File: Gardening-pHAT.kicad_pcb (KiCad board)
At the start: 2 copper layers, 65 x 30 mm, 25 parts, among them P1 CONN_01X03, P2 CONN_01X03, P3 CONN_01X03, P4 CONN_02X05, U1 CAT24C32WI-GT3, U2 MCP3002

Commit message: Control 3.3V to sensors through GPIO
Connect the 3.3V of the soil moisture sensors
to GPIO5 and GPIO6 of Raspberry Pi. This way
the sensors will be enabled only during
measurement and their life will be significantly
increased.

Signed-off-by: Leon Anavi <leon@anavi.org>
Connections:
- P2 pad 3: +3V3 -> /GPIO6
- P3 pad 3: +3V3 -> /GPIO5
- RASP_CONN1 pad 29: (no net) -> /GPIO5
- RASP_CONN1 pad 31: (no net) -> /GPIO6
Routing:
- net /GPIO5: track 0.00 -> 25.5 mm
- net /GPIO6: track 0.00 -> 25.1 mm
- net +3V3: track 170.8 -> 157.5 mm
- net Net-(RASP_CONN1-Pad19): track 22.8 -> 21.3 mm
- net Net-(R3-Pad2): track 35.5 -> 35.0 mm
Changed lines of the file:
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@@
     (thickness 1.6)
     (drawings 32)
-    (tracks 267)
+    (tracks 273)
     (zones 0)
     (modules 25)
-    (nets 23)
+    (nets 25)
   )
   (page A4)
@@
   (net 21 "Net-(D1-Pad2)")
   (net 22 "Net-(R4-Pad2)")
+  (net 23 /GPIO6)
+  (net 24 /GPIO5)
   (net_class Default "This is the default net class."
     (clearance 0.254)
@@
     (add_net +3V3)
     (add_net +5V)
+    (add_net /GPIO5)
+    (add_net /GPIO6)
     (add_net /RXD)
     (add_net /TXD)
@@
       (net 2 GND))
     (pad 3 thru_hole circle (at 10 3.5) (size 3 3) (drill 1.4) (layers *.Cu *.Mask F.SilkS)
-      (net 1 +3V3))
+      (net 23 /GPIO6))
   )
   (module Pin_Headers:Pin_Header_Straight_1x04 (layer F.Cu)
@@
     (pad 28 thru_hole oval (at 2.54 33.02 90) (size 1.7272 1.7272) (drill 1.016) (layers *.Cu *.Mask F.SilkS)
       (net 5 "Net-(R2-Pad2)"))
-    (pad 29 thru_hole oval (at 0 35.56 90) (size 1.7272 1.7272) (drill 1.016) (layers *.Cu *.Mask F.SilkS))
+    (pad 29 thru_hole oval (at 0 35.56 90) (size 1.7272 1.7272) (drill 1.016) (layers *.Cu *.Mask F.SilkS)
+      (net 24 /GPIO5))
     (pad 30 thru_hole oval (at 2.54 35.56 90) (size 1.7272 1.7272) (drill 1.016) (layers *.Cu *.Mask F.SilkS)
       (net 2 GND))
-    (pad 31 thru_hole oval (at 0 38.1 90) (size 1.7272 1.7272) (drill 1.016) (layers *.Cu *.Mask F.SilkS))
+    (pad 31 thru_hole oval (at 0 38.1 90) (size 1.7272 1.7272) (drill 1.016) (layers *.Cu *.Mask F.SilkS)
+      (net 23 /GPIO6))
     (pad 32 thru_hole oval (at 2.54 38.1 90) (size 1.7272 1.7272) (drill 1.016) (layers *.Cu *.Mask F.SilkS))
     (pad 33 thru_hole oval (at 0 40.64 90) (size 1.7272 1.7272) (drill 1.016) (layers *.Cu *.Mask F.SilkS))
@@
       (net 2 GND))
     (pad 3 thru_hole circle (at 10 3.5) (size 3 3) (drill 1.4) (layers *.Cu *.Mask F.SilkS)
-      (net 1 +3V3))
+      (net 24 /GPIO5))
   )
   (module myfootprint:KLEMA_1x3 (layer F.Cu)
@@
   (gr_arc (start 151.5011 102.0036) (end 148.5011 102.0036) (angle -90) (layer Edge.Cuts) (width 0.1))
   (gr_circle (center 152.0011 101.5036) (end 152.0011 101.5036) (layer Edge.Cuts) (width 0.1))
+  (segment (start 204.2795 84.455) (end 204.2795 85.0265) (width 0.5) (layer F.Cu) (net 1))
+  (segment (start 204.2795 85.0265) (end 199.898 89.408) (width 0.5) (layer F.Cu) (net 1))
+  (segment (start 176.6165 103.886) (end 173.8935 101.163) (width 0.5) (layer F.Cu) (net 1))
+  (segment (start 195.199 103.886) (end 176.6165 103.886) (width 0.5) (layer F.Cu) (net 1))
+  (segment (start 196.469 102.616) (end 195.199 103.886) (width 0.5) (layer F.Cu) (net 1))
+  (segment (start 196.469 99.695) (end 196.469 102.616) (width 0.5) (layer F.Cu) (net 1))
+  (segment (start 199.898 96.266) (end 196.469 99.695) (width 0.5) (layer F.Cu) (net 1))
+  (segment (start 199.898 89.408) (end 199.898 96.266) (width 0.5) (layer F.Cu) (net 1))
   (segment (start 159.893 93.134) (end 171.8905 93.134) (width 0.5) (layer F.Cu) (net 1))
   (segment (start 171.8905 93.134) (end 171.9335 93.091) (width 0.5) (layer F.Cu) (net 1))
@@
   (segment (start 157.7135 90.9545) (end 159.893 93.134) (width 0.5) (layer F.Cu) (net 1))
   (segment (start 159.893 93.134) (end 159.893 93.218) (width 0.5) (layer F.Cu) (net 1) (status 30))
-  (segment (start 173.934 101.163) (end 176.657 103.886) (width 0.5) (layer B.Cu) (net 1))
-  (segment (start 176.657 103.886) (end 186.22 103.886) (width 0.5) (layer B.Cu) (net 1))
-  (segment (start 186.22 103.886) (end 188.943 101.163) (width 0.5) (layer B.Cu) (net 1))
-  (segment (start 188.943 101.694) (end 191.135 103.886) (width 0.5) (layer B.Cu) (net 1))
-  (segment (start 201.333 103.886) (end 204.056 101.163) (width 0.5) (layer B.Cu) (net 1))
-  (segment (start 191.135 103.886) (end 201.333 103.886) (width 0.5) (layer B.Cu) (net 1))
-  (segment (start 204.056 101.163) (end 204.056 94.836) (width 0.5) (layer B.Cu) (net 1))
-  (segment (start 200.025 84.455) (end 204.2795 84.455) (width 0.5) (layer B.Cu) (net 1))
-  (segment (start 198.374 86.106) (end 200.025 84.455) (width 0.5) (layer B.Cu) (net 1))
-  (segment (start 198.374 89.154) (end 198.374 86.106) (width 0.5) (layer B.Cu) (net 1))
-  (segment (start 204.056 94.836) (end 198.374 89.154) (width 0.5) (layer B.Cu) (net 1))
   (segment (start 173.8935 101.163) (end 173.934 101.163) (width 0.5) (layer B.Cu) (net 1))
-  (segment (start 188.943 101.163) (end 188.943 101.694) (width 0.5) (layer B.Cu) (net 1))
   (segment (start 208.788 85.936) (end 208.788 88.816) (width 0.5) (layer F.Cu) (net 1))
   (segment (start 177.17 79.8) (end 177.17 88.8415) (width 0.5) (layer B.Cu) (net 1))
@@
   (segment (start 208.788 91.016) (end 204.3635 89.619) (width 0.5) (layer F.Cu) (net 5) (status 10))
   (segment (start 204.3635 89.619) (end 204.2795 89.535) (width 0.5) (layer F.Cu) (net 5) (status 30))
+  (segment (start 189.87 79.8) (end 189.87 81.158) (width 0.5) (layer F.Cu) (net 6))
+  (segment (start 202.184 89.9795) (end 204.2795 92.075) (width 0.5) (layer B.Cu) (net 6))
+  (segment (start 202.184 85.598) (end 202.184 89.9795) (width 0.5) (layer B.Cu) (net 6))
+  (segment (start 201.549 84.963) (end 202.184 85.598) (width 0.5) (layer B.Cu) (net 6))
+  (via (at 201.549 84.963) (size 0.85) (drill 0.4) (layers F.Cu B.Cu) (net 6))
+  (segment (start 198.628 82.042) (end 201.549 84.963) (width 0.5) (layer F.Cu) (net 6))
+  (segment (start 190.754 82.042) (end 198.628 82.042) (width 0.5) (layer F.Cu) (net 6))
+  (segment (start 189.87 81.158) (end 190.754 82.042) (width 0.5) (layer F.Cu) (net 6))
   (segment (start 204.2795 92.075) (end 204.343 92.075) (width 0.5) (layer B.Cu) (net 6))
   (segment (start 204.343 92.075) (end 210.312 86.106) (width 0.5) (layer B.Cu) (net 6))
@@
   (via (at 210.312 86.106) (size 0.85) (drill 0.4) (layers F.Cu B.Cu) (net 6))
   (segment (start 204.2795 92.075) (end 204.2795 91.8845) (width 0.5) (layer B.Cu) (net 6) (status 30))
-  (segment (start 204.2795 91.8845) (end 199.39 87.5665) (width 0.5) (layer B.Cu) (net 6) (status 10))
-  (segment (start 199.3265 87.503) (end 199.3265 82.6565) (width 0.5) (layer F.Cu) (net 6))
-  (segment (start 199.39 87.5665) (end 199.3265 87.503) (width 0.5) (layer F.Cu) (net 6))
-  (via (at 199.39 87.5665) (size 0.85) (drill 0.4) (layers F.Cu B.Cu) (net 6))
   (segment (start 204.2795 92.075) (end 204.2795 92.0115) (width 0.5) (layer B.Cu) (net 6) (status 30))
-  (segment (start 189.87 79.8) (end 189.87 81.9835) (width 0.5) (layer F.Cu) (net 6))
-  (segment (start 190.543 82.6565) (end 199.3265 82.6565) (width 0.5) (layer F.Cu) (net 6))
-  (segment (start 189.87 81.9835) (end 190.543 82.6565) (width 0.5) (layer F.Cu) (net 6))
   (segment (start 189.865 79.756) (end 189.87 79.8) (width 0.5) (layer F.Cu) (net 6) (status 80000))
   (segment (start 164.3135 84.448) (end 164.2745 84.455) (width 0.5) (layer B.Cu) (net 7) (status 80000))
@@
   (segment (start 167.01 77.26) (end 167.3665 77.26) (width 0.254) (layer F.Cu) (net 10))
   (segment (start 167.01 77.26) (end 167.31 77.26) (width 0.254) (layer F.Cu) (net 10))
-  (segment (start 179.71 79.8) (end 179.71 81.412) (width 0.5) (layer B.Cu) (net 11))
-  (segment (start 179.71 81.412) (end 184.9755 86.6775) (width 0.5) (layer B.Cu) (net 11))
-  (segment (start 184.9755 86.6775) (end 188.849 86.6775) (width 0.5) (layer B.Cu) (net 11))
-  (segment (start 188.849 86.6775) (end 188.849 88.011) (width 0.5) (layer B.Cu) (net 11))
-  (segment (start 188.849 88.011) (end 190.373 89.535) (width 0.5) (layer B.Cu) (net 11))
-  (segment (start 190.373 89.535) (end 194.31 89.535) (width 0.5) (layer B.Cu) (net 11))
-  (via (at 194.31 89.535) (size 0.85) (drill 0.4) (layers F.Cu B.Cu) (net 11))
-  (segment (start 194.31 89.535) (end 194.3735 89.4715) (width 0.5) (layer F.Cu) (net 11))
-  (segment (start 194.3735 89.4715) (end 194.3735 87.1093) (width 0.5) (layer F.Cu) (net 11))
+  (segment (start 179.71 79.8) (end 179.71 81.031) (width 0.5) (layer B.Cu) (net 11))
+  (segment (start 194.3735 88.3285) (end 194.3735 87.1093) (width 0.5) (layer F.Cu) (net 11))
+  (segment (start 192.913 89.789) (end 194.3735 88.3285) (width 0.5) (layer F.Cu) (net 11))
+  (segment (start 191.516 89.789) (end 192.913 89.789) (width 0.5) (layer F.Cu) (net 11))
+  (segment (start 191.389 89.662) (end 191.516 89.789) (width 0.5) (layer F.Cu) (net 11))
+  (via (at 191.389 89.662) (size 0.85) (drill 0.4) (layers F.Cu B.Cu) (net 11))
+  (segment (start 188.468 86.741) (end 191.389 89.662) (width 0.5) (layer B.Cu) (net 11))
+  (segment (start 185.42 86.741) (end 188.468 86.741) (width 0.5) (layer B.Cu) (net 11))
+  (segment (start 179.71 81.031) (end 185.42 86.741) (width 0.5) (layer B.Cu) (net 11))
   (segment (start 182.25 79.8) (end 182.289 79.8) (width 0.5) (layer F.Cu) (net 12))
   (segment (start 182.25 79.8) (end 182.25 80.015) (width 0.5) (layer B.Cu) (net 12))
@@
   (segment (start 157.607 93.134) (end 157.564 93.134) (width 0.5) (layer F.Cu) (net 22))
   (segment (start 174.63 79.8) (end 174.63 80.015) (width 0.5) (layer B.Cu) (net 22))
+  (segment (start 194.95 79.8) (end 194.95 80.015) (width 0.5) (layer B.Cu) (net 23))
+  (segment (start 194.95 80.015) (end 198.247 83.312) (width 0.5) (layer B.Cu) (net 23))
+  (segment (start 198.247 83.312) (end 198.247 95.354) (width 0.5) (layer B.Cu) (net 23))
+  (segment (start 198.247 95.354) (end 204.056 101.163) (width 0.5) (layer B.Cu) (net 23))
+  (segment (start 192.41 79.8) (end 192.41 81.92) (width 0.5) (layer B.Cu) (net 24))
+  (segment (start 195.072 95.034) (end 188.943 101.163) (width 0.5) (layer B.Cu) (net 24))
+  (segment (start 195.072 84.582) (end 195.072 95.034) (width 0.5) (layer B.Cu) (net 24))
+  (segment (start 192.41 81.92) (end 195.072 84.582) (width 0.5) (layer B.Cu) (net 24))
+  (segment (start 188.943 101.163) (end 188.943 101.694) (width 0.5) (layer B.Cu) (net 24))
   (zone (net 2) (net_name GND) (layer F.Cu) (hatch edge 0.508)
     (connect_pads (clearance 0.508))

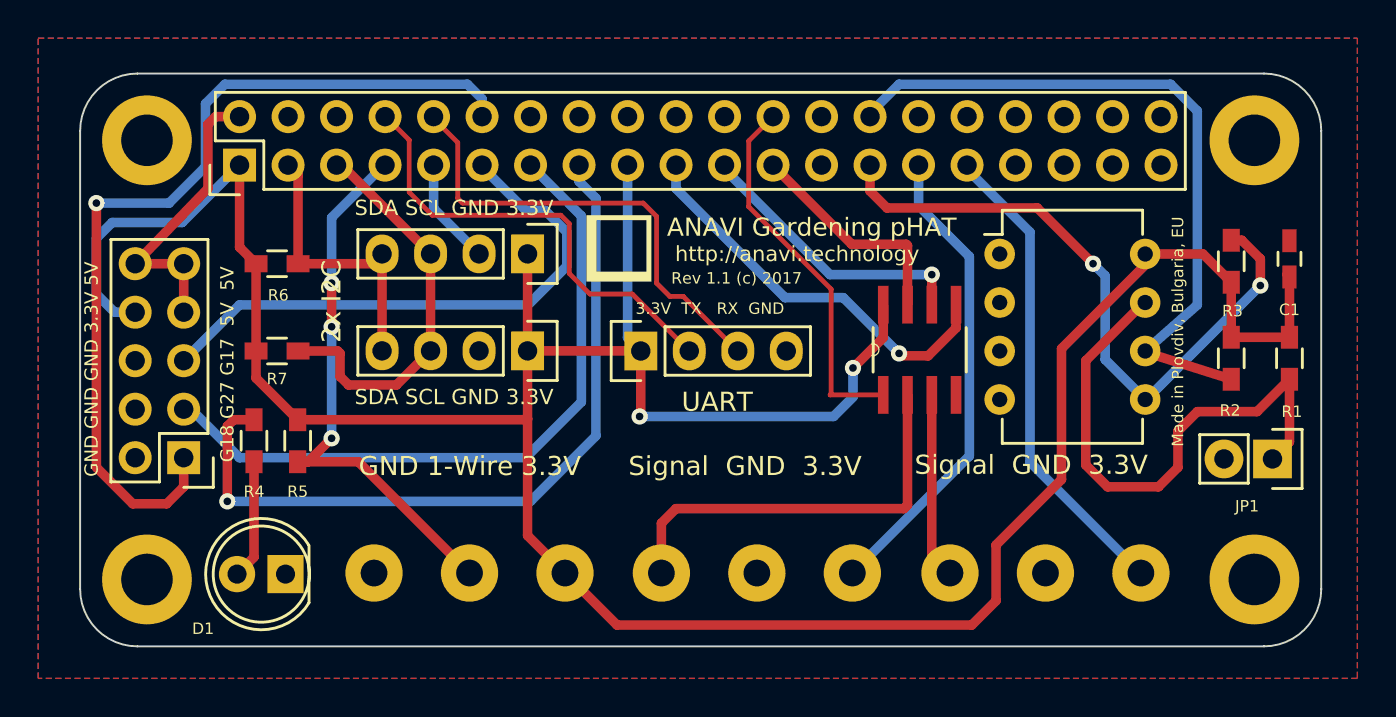
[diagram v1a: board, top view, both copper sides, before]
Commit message: Gardening-pHAT: Update tracks
Update tracks and labels.

Signed-off-by: Leon Anavi <leon@anavi.org>
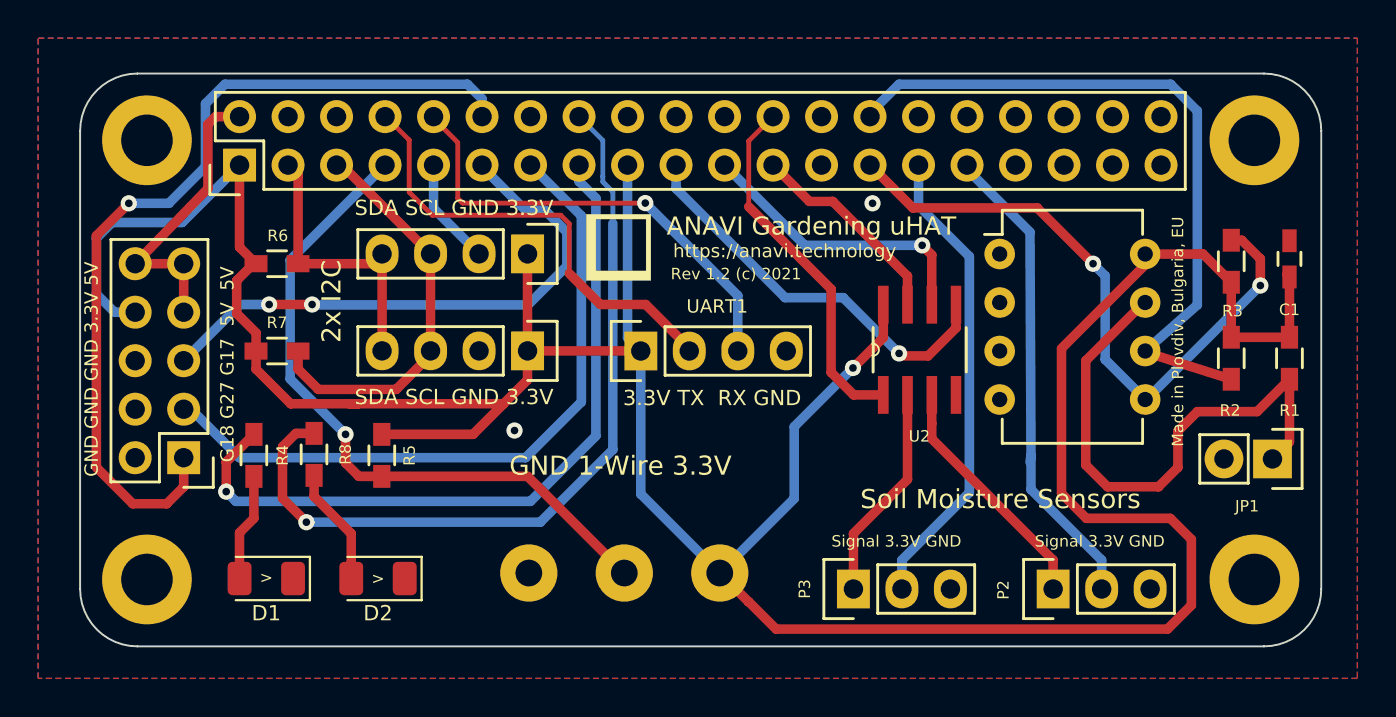
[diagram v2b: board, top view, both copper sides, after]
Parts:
- added D2: LED, LED_SMD:LED_1206_3216Metric, F.Cu at (164.1, 101.5)
- added R8: 270R, Resistors_SMD:R_0603_HandSoldering, F.Cu at (160.8, 95.0)
- D1: footprint LEDs:LED-5MM -> LED_SMD:LED_1206_3216Metric
- P2, P3: footprint myfootprint:KLEMA_1x3 -> Pin_Headers:Pin_Header_Straight_1x03
- moved P3 11.0 mm to (189.0, 102.0), turned to 90 degrees
- moved P1 8.11 mm to (172.0, 97.7)
- moved P2 6.93 mm to (199.5, 102.0), turned to 90 degrees
- moved R5 4.47 mm to (164.3, 95.0)
- moved D1 1.03 mm to (158.2, 101.5)
- moved R4 0.77 mm to (157.6, 95.0)
- moved ? 0.05 mm to (176.7, 84.2)
- renumbered UART to UART1
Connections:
- P2 pad 2: GND -> /GPIO6
- P2 pad 3: /GPIO6 -> GND
- P3 pad 2: GND -> /GPIO5
- P3 pad 3: /GPIO5 -> GND
- RASP_CONN1 pad 16: (no net) -> Net-(R8-Pad2)
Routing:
- net Net-(R8-Pad2): track 0.00 -> 42.2 mm, vias 0 -> 1
- net +3V3: track 157.5 -> 171.4 mm, vias 2 -> 1
- net Net-(P3-Pad1): track 21.7 -> 11.9 mm
- net Net-(P1-Pad2): track 30.3 -> 37.4 mm, vias 3 -> 1
- net Net-(D2-Pad2): track 0.00 -> 6.21 mm
- net Net-(P2-Pad1): track 9.72 -> 12.8 mm
- net Net-(R4-Pad2): track 41.0 -> 39.4 mm
- net Net-(D1-Pad2): track 6.79 -> 5.66 mm
- net Net-(P4-Pad1): track 47.1 -> 46.1 mm
- net Net-(RASP_CONN1-Pad23): track 11.9 -> 11.0 mm
- net Net-(R3-Pad2): track 35.0 -> 34.2 mm
- net /GPIO5: track 25.5 -> 24.8 mm
- net Net-(RASP_CONN1-Pad24): track 19.7 -> 19.0 mm
- net Net-(RASP_CONN1-Pad21): track 15.0 -> 15.7 mm
- net /RXD: track 25.8 -> 25.6 mm, vias 0 -> 1
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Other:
- board text added: ">"
- board text added: "ANAVI Gardening uHAT"
- board text added: "Rev 1.2 (c) 2021"
- board text added: "Signal 3.3V GND"
- board text added: "Soil Moisture Sensors"
- board text added: "https://anavi.technology"
- board text removed: "ANAVI Gardening pHAT"
- board text removed: "Rev 1.1 (c) 2017"
- board text removed: "Signal GND 3.3V"
- board text removed: "http://anavi.technology"

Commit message: Add fabrication labels for assemly
Create additional labels on the fabrication layer to help with
the SMT assembly of the PCB.

Signed-off-by: Leon Anavi <leon@anavi.org>
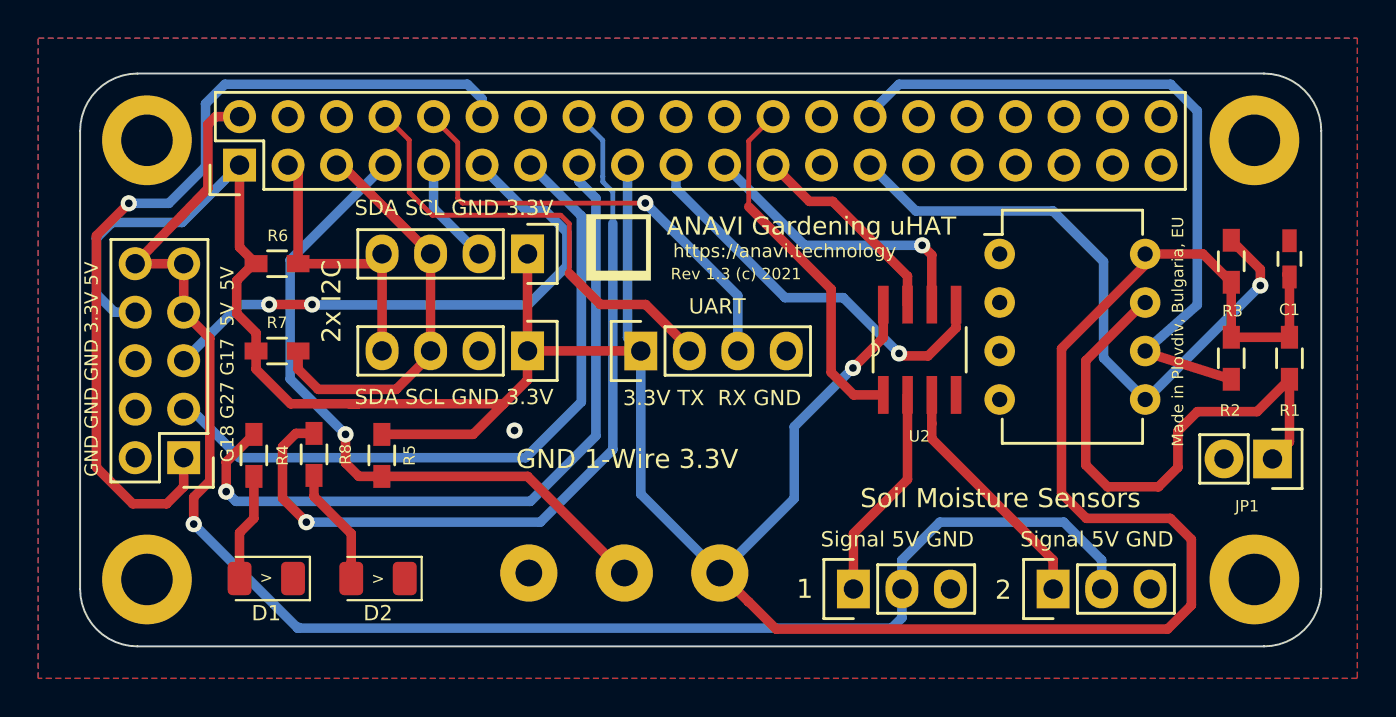
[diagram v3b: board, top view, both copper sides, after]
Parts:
- D1: value LED -> KP-3216EC
- D2: value LED -> KP-3216SGC
- renumbered P3 to 1, P2 to 2, UART1 to UART
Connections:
- 1 pad 2: /GPIO5 -> +5V
- 2 pad 2: /GPIO6 -> +5V
- RASP_CONN1 pad 29: /GPIO5 -> (no net)
- RASP_CONN1 pad 31: /GPIO6 -> (no net)
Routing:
- net +5V: track 15.8 -> 84.1 mm, vias 0 -> 1
- net /GPIO6: track 25.5 -> 0.00 mm
- net /GPIO5: track 24.8 -> 0.00 mm
- net Net-(R3-Pad2): track 34.2 -> 34.3 mm, vias 2 -> 1
- net GND: vias 2 -> 1
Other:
- board text added: "MCP3002-I/SN"
- board text added: "Rev 1.3 (c) 2021"
- board text added: "Signal 5V GND"
- board text removed: "Rev 1.2 (c) 2021"
- board text removed: "Signal 3.3V GND"
